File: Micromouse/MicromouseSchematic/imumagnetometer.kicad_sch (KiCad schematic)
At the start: 13 parts, among them U3 ICM-42688-P, U4 LIS2MDLTR

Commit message: assigned capacitor footprints. still have to figure out rest
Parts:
- C38, C5, C6: footprint (none) -> Capacitor_SMD:C_0402_1005Metric
- C39, C40: footprint (none) -> Capacitor_SMD:C_0603_1608Metric
- C4: footprint (none) -> Capacitor_SMD:C_0201_0603Metric
- C7: footprint (none) -> Capacitor_SMD:C_0805_2012Metric
- R23, R24, R26, R27: footprint (none) -> Resistor_SMD:R_0402_1005Metric
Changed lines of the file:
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@@
 			)
 		)
-		(property "Footprint" ""
+		(property "Footprint" "Capacitor_SMD:C_0402_1005Metric"
 			(at 262.89 65.0748 0)
 			(effects
@@
 			)
 		)
-		(property "Footprint" ""
+		(property "Footprint" "Capacitor_SMD:C_0603_1608Metric"
 			(at 144.4752 77.47 0)
 			(effects
@@
 			)
 		)
-		(property "Footprint" ""
+		(property "Footprint" "Resistor_SMD:R_0402_1005Metric"
 			(at 73.152 69.85 90)
 			(effects
@@
 			)
 		)
-		(property "Footprint" ""
+		(property "Footprint" "Resistor_SMD:R_0402_1005Metric"
 			(at 188.722 69.85 90)
 			(effects
@@
 			)
 		)
-		(property "Footprint" ""
+		(property "Footprint" "Resistor_SMD:R_0402_1005Metric"
 			(at 200.152 69.85 90)
 			(effects
@@
 			)
 		)
-		(property "Footprint" ""
+		(property "Footprint" "Capacitor_SMD:C_0402_1005Metric"
 			(at 160.9852 74.93 0)
 			(effects
@@
 			)
 		)
-		(property "Footprint" ""
+		(property "Footprint" "Capacitor_SMD:C_0402_1005Metric"
 			(at 271.78 75.2348 0)
 			(effects
@@
 			)
 		)
-		(property "Footprint" ""
+		(property "Footprint" "Capacitor_SMD:C_0603_1608Metric"
 			(at 172.4152 74.93 0)
 			(effects
@@
 			)
 		)
-		(property "Footprint" ""
+		(property "Footprint" "Resistor_SMD:R_0402_1005Metric"
 			(at 61.722 69.85 90)
 			(effects
@@
 			)
 		)
-		(property "Footprint" ""
+		(property "Footprint" "Capacitor_SMD:C_0805_2012Metric"
 			(at 271.78 86.6648 0)
 			(effects
@@
 			)
 		)
-		(property "Footprint" ""
+		(property "Footprint" "Capacitor_SMD:C_0201_0603Metric"
 			(at 256.54 80.3148 0)
 			(effects

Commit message: added resistors, must need to add capacitors
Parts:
- C38, C5, C6: footprint Capacitor_SMD:C_0402_1005Metric -> (none)
- C39, C40: footprint Capacitor_SMD:C_0603_1608Metric -> (none)
- C4: footprint Capacitor_SMD:C_0201_0603Metric -> (none)
- C7: footprint Capacitor_SMD:C_0805_2012Metric -> (none)
- R23, R24, R26, R27: footprint Resistor_SMD:R_0402_1005Metric -> Resistor_SMD:R_0603_1608Metric
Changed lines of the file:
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@@
 			)
 		)
-		(property "Footprint" "Capacitor_SMD:C_0402_1005Metric"
+		(property "Footprint" ""
 			(at 262.89 65.0748 0)
 			(effects
@@
 			)
 		)
-		(property "Footprint" "Capacitor_SMD:C_0603_1608Metric"
+		(property "Footprint" ""
 			(at 144.4752 77.47 0)
 			(effects
@@
 			)
 		)
-		(property "Footprint" "Resistor_SMD:R_0402_1005Metric"
+		(property "Footprint" "Resistor_SMD:R_0603_1608Metric"
 			(at 73.152 69.85 90)
 			(effects
@@
 			)
 		)
-		(property "Footprint" "Resistor_SMD:R_0402_1005Metric"
+		(property "Footprint" "Resistor_SMD:R_0603_1608Metric"
 			(at 188.722 69.85 90)
 			(effects
@@
 			)
 		)
-		(property "Footprint" "Resistor_SMD:R_0402_1005Metric"
+		(property "Footprint" "Resistor_SMD:R_0603_1608Metric"
 			(at 200.152 69.85 90)
 			(effects
@@
 			)
 		)
-		(property "Footprint" "Capacitor_SMD:C_0402_1005Metric"
+		(property "Footprint" ""
 			(at 160.9852 74.93 0)
 			(effects
@@
 			)
 		)
-		(property "Footprint" "Capacitor_SMD:C_0402_1005Metric"
+		(property "Footprint" ""
 			(at 271.78 75.2348 0)
 			(effects
@@
 			)
 		)
-		(property "Footprint" "Capacitor_SMD:C_0603_1608Metric"
+		(property "Footprint" ""
 			(at 172.4152 74.93 0)
 			(effects
@@
 			)
 		)
-		(property "Footprint" "Resistor_SMD:R_0402_1005Metric"
+		(property "Footprint" "Resistor_SMD:R_0603_1608Metric"
 			(at 61.722 69.85 90)
 			(effects
@@
 			)
 		)
-		(property "Footprint" "Capacitor_SMD:C_0805_2012Metric"
+		(property "Footprint" ""
 			(at 271.78 86.6648 0)
 			(effects
@@
 			)
 		)
-		(property "Footprint" "Capacitor_SMD:C_0201_0603Metric"
+		(property "Footprint" ""
 			(at 256.54 80.3148 0)
 			(effects

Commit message: Changd IR sensors and emmiters to 5mm LEDs
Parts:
- C38, C39, C4, C40, C5, C6, C7: footprint (none) -> Capacitor_SMD:C_0402_1005Metric
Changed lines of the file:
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@@
 			)
 		)
-		(property "Footprint" ""
+		(property "Footprint" "Capacitor_SMD:C_0402_1005Metric"
 			(at 262.89 65.0748 0)
 			(effects
@@
 			)
 		)
-		(property "Footprint" ""
+		(property "Footprint" "Capacitor_SMD:C_0402_1005Metric"
 			(at 144.4752 77.47 0)
 			(effects
@@
 			)
 		)
-		(property "Footprint" ""
+		(property "Footprint" "Capacitor_SMD:C_0402_1005Metric"
 			(at 160.9852 74.93 0)
 			(effects
@@
 			)
 		)
-		(property "Footprint" ""
+		(property "Footprint" "Capacitor_SMD:C_0402_1005Metric"
 			(at 271.78 75.2348 0)
 			(effects
@@
 			)
 		)
-		(property "Footprint" ""
+		(property "Footprint" "Capacitor_SMD:C_0402_1005Metric"
 			(at 172.4152 74.93 0)
 			(effects
@@
 			)
 		)
-		(property "Footprint" ""
+		(property "Footprint" "Capacitor_SMD:C_0402_1005Metric"
 			(at 271.78 86.6648 0)
 			(effects
@@
 			)
 		)
-		(property "Footprint" ""
+		(property "Footprint" "Capacitor_SMD:C_0402_1005Metric"
 			(at 256.54 80.3148 0)
 			(effects

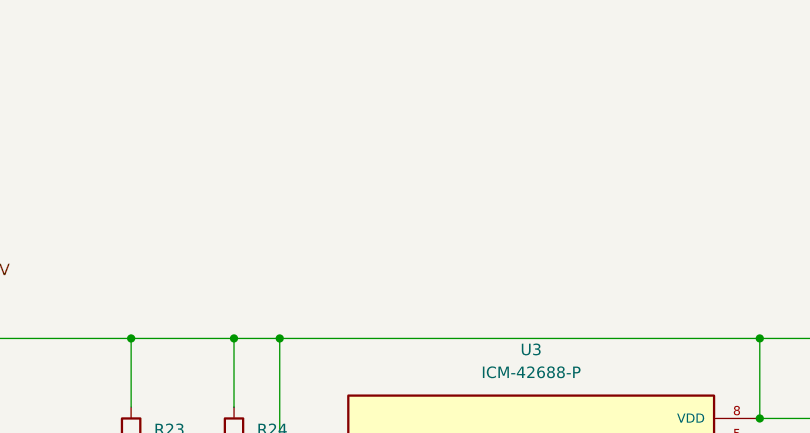
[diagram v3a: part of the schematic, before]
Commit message: to-do IMU+Mag figure it out or mutli layer pcb?
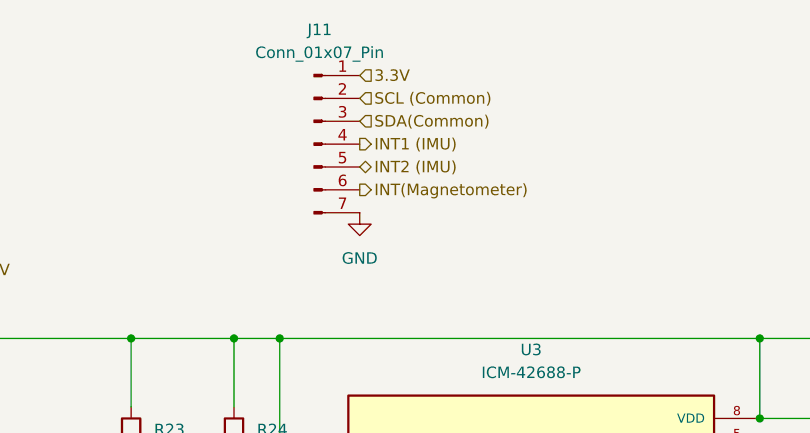
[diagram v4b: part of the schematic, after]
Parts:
- added J11: Conn_01x07_Pin, Connector_JST:JST_ZH_B7B-ZR_1x07_P1.50mm_Vertical, symbol Connector:Conn_01x07_Pin
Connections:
- net 3.3V: now also J11.1 (Pin_1)
- net GND: now also J11.7 (Pin_7)
- net INT(Magnetometer): now also J11.6 (Pin_6)
- net INT1 (IMU): now also J11.4 (Pin_4)
- net INT2 (IMU): now also J11.5 (Pin_5)
- net SCL (Common): now also J11.2 (Pin_2)
- net SDA(Common): now also J11.3 (Pin_3)
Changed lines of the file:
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@@
+	(hierarchical_label "INT2 (IMU)"
+		(shape bidirectional)
+		(at 88.9 39.37 0)
+		(effects
+			(font
+				(size 1.27 1.27)
+			)
+			(justify left)
+		)
+	)
 	(hierarchical_label "INT2 (IMU)"
 		(shape bidirectional)
@@
 		)
 	)
+	(hierarchical_label "INT(Magnetometer)"
+		(shape output)
+		(at 88.9 41.91 0)
+		(effects
+			(font
+				(size 1.27 1.27)
+			)
+			(justify left)
+		)
+	)
 	(hierarchical_label "SDA(Common)"
 		(shape input)
@@
 	(hierarchical_label "SCL (Common)"
 		(shape input)
+		(at 88.9 31.75 0)
+		(effects
+			(font
+				(size 1.27 1.27)
+			)
+			(justify left)
+		)
+	)
+	(hierarchical_label "SDA(Common)"
+		(shape input)
+		(at 88.9 34.29 0)
+		(effects
+			(font
+				(size 1.27 1.27)
+			)
+			(justify left)
+		)
+	)
+	(hierarchical_label "3.3V"
+		(shape input)
+		(at 88.9 29.21 0)
+		(effects
+			(font
+				(size 1.27 1.27)
+			)
+			(justify left)
+		)
+	)
+	(hierarchical_label "INT1 (IMU)"
+		(shape output)
+		(at 88.9 36.83 0)
+		(effects
+			(font
+				(size 1.27 1.27)
+			)
+			(justify left)
+		)
+	)
+	(hierarchical_label "SCL (Common)"
+		(shape input)
 		(at 34.29 82.55 180)
 		(effects
@@
 	)
 	(symbol
+		(lib_id "Connector:Conn_01x07_Pin")
+		(at 83.82 36.83 0)
+		(unit 1)
+		(exclude_from_sim no)
+		(in_bom yes)
+		(on_board yes)
+		(dnp no)
+		(fields_autoplaced yes)
+		(property "Reference" "J11"
+			(at 84.455 24.13 0)
+			(effects
+				(font
+					(size 1.27 1.27)
+				)
+			)
+		)
+		(property "Value" "Conn_01x07_Pin"
+			(at 84.455 26.67 0)
+			(effects
+				(font
+					(size 1.27 1.27)
+				)
+			)
+		)
+		(property "Footprint" "Connector_JST:JST_ZH_B7B-ZR_1x07_P1.50mm_Vertical"
+			(at 83.82 36.83 0)
+			(effects
+				(font
+					(size 1.27 1.27)
+				)
+				(hide yes)
+			)
+		)
+		(property "Datasheet" "~"
+			(at 83.82 36.83 0)
+			(effects
+				(font
+					(size 1.27 1.27)
+				)
+				(hide yes)
+			)
+		)
+		(property "Description" "Generic connector, single row, 01x07, script generated"
+			(at 83.82 36.83 0)
+			(effects
+				(font
+					(size 1.27 1.27)
+				)
+				(hide yes)
+			)
+		)
+		(pin "3"
+		)
+		(pin "2"
+		)
+		(pin "1"
+		)
+		(pin "7"
+		)
+		(pin "5"
+		)
+		(pin "4"
+		)
+		(pin "6"
+		)
+		(instances
+			(project ""
+				(path "/0dcfab91-6b00-43c0-ac0b-8c301cb559e5/020b5f85-8a9d-45f7-80e4-737602419b71"
+					(reference "J11")
+					(unit 1)
+				)
+			)
+		)
+	)
+	(symbol
 		(lib_id "power:GND")
 		(at 256.54 101.6 0)
@@
 					(unit 1)
 				)
+			)
+		)
+	)
+	(symbol
+		(lib_id "power:GND")
+		(at 88.9 44.45 0)
+		(unit 1)
+		(exclude_from_sim no)
+		(in_bom yes)
+		(on_board yes)
+		(dnp no)
+		(fields_autoplaced yes)
+		(property "Reference" "#PWR015"
+			(at 88.9 50.8 0)
+			(effects
+				(font
+					(size 1.27 1.27)
+				)
+				(hide yes)
+			)
+		)
+		(property "Value" "GND"
+			(at 88.9 49.53 0)
+			(effects
+				(font
+					(size 1.27 1.27)
+				)
+			)
+		)
+		(property "Footprint" ""
+			(at 88.9 44.45 0)
+			(effects
+				(font
+					(size 1.27 1.27)
+				)
+				(hide yes)
+			)
+		)
+		(property "Datasheet" ""
+			(at 88.9 44.45 0)
+			(effects
+				(font
+					(size 1.27 1.27)
+				)
+				(hide yes)
+			)
+		)
+		(property "Description" "Power symbol creates a global label with name \"GND\" , ground"
+			(at 88.9 44.45 0)
+			(effects
+				(font
+					(size 1.27 1.27)
+				)
+				(hide yes)
+			)
+		)
+		(pin "1"
+		)
+		(instances
+			(project "MicromouseSchematic"
+				(path "/0dcfab91-6b00-43c0-ac0b-8c301cb559e5/020b5f85-8a9d-45f7-80e4-737602419b71"
+					(reference "#PWR015")
+					(unit 1)
+				)
